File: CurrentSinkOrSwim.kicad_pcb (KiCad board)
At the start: 2 copper layers, 22 parts, among them P101 CONN_01X02, P102 CONN_01X03, P103 CONN_01X02, Q401 BUK9575, U201 LMV358, U301 LM2931D-R

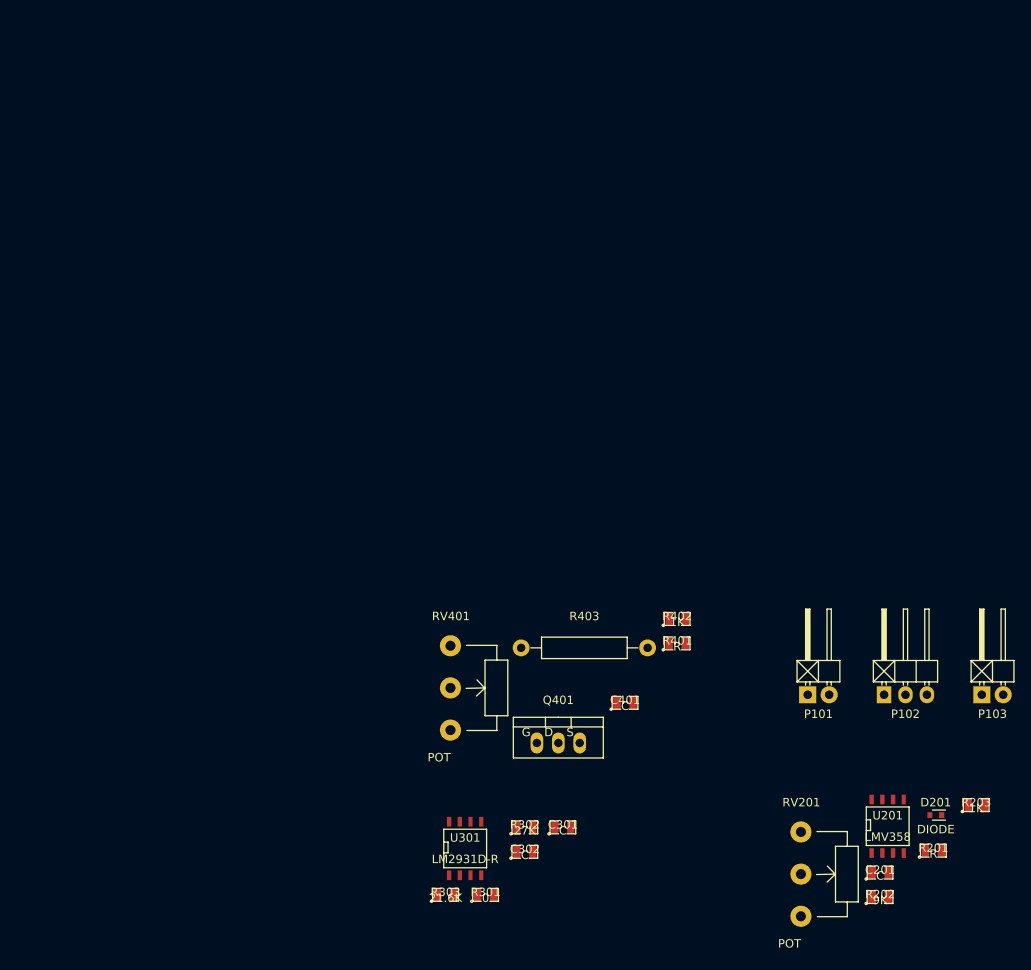
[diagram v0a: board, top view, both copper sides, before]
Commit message: Added board outline
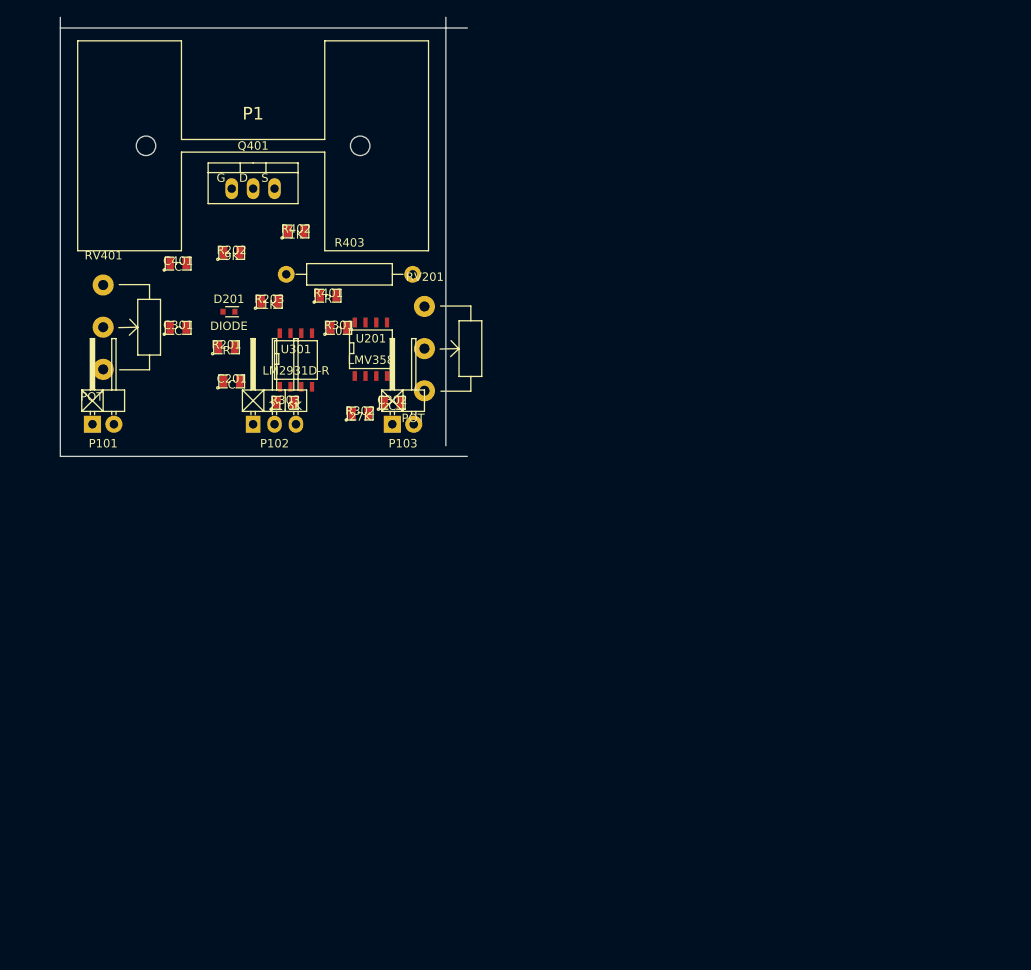
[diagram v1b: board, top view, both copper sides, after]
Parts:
- added P1: CONN_01X01, Current:FA-T220-38E, F.Cu at (127.0, 48.3)
- moved R202 108.4 mm to (124.5, 61.0)
- moved D201 102.9 mm to (124.1, 67.9)
- moved R201 102.9 mm to (123.8, 72.2)
- moved R203 102.9 mm to (128.9, 66.8)
- moved C201 96.5 mm to (124.5, 76.2)
- moved P101 90.7 mm to (109.2, 81.3)
- moved U201 83.4 mm to (141.0, 72.4)
- moved P102 81.4 mm to (129.5, 81.3)
- moved P103 76.9 mm to (144.8, 81.3)
- moved RV201 76.7 mm to (147.3, 67.3)
- moved Q401 75.0 mm to (127.0, 53.3)
- moved C301 74.8 mm to (118.1, 69.8)
- moved C401 74.3 mm to (118.1, 62.2)
- moved R301 69.5 mm to (137.2, 69.8)
- moved R402 64.5 mm to (132.1, 58.4)
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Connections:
- R302 pad 1: Net-(R302-Pad1) -> 2.7V
- U301 pad 5: Net-(U301-Pad5) -> Net-(R301-Pad1)
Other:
- board outline added: 48.3 x 52.1 mm

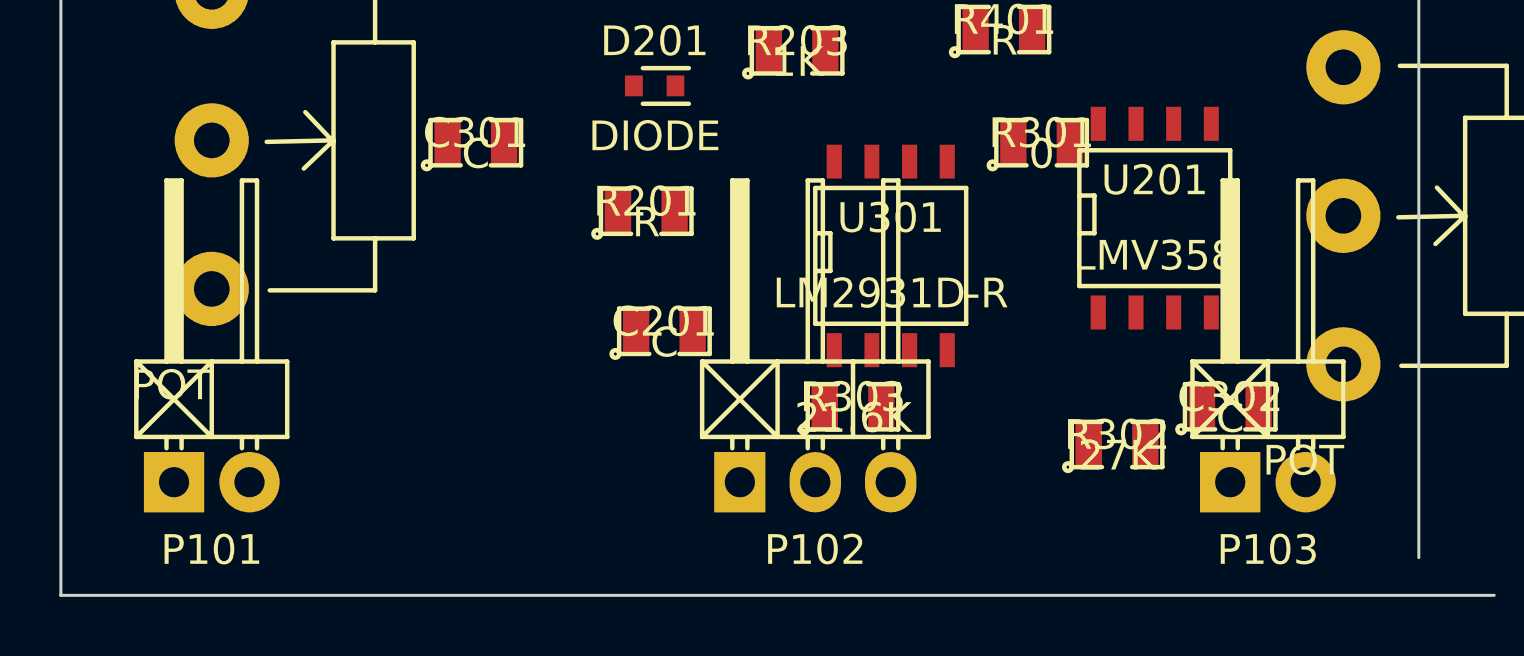
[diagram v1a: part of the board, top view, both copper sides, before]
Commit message: Replacing the terminal block footprints
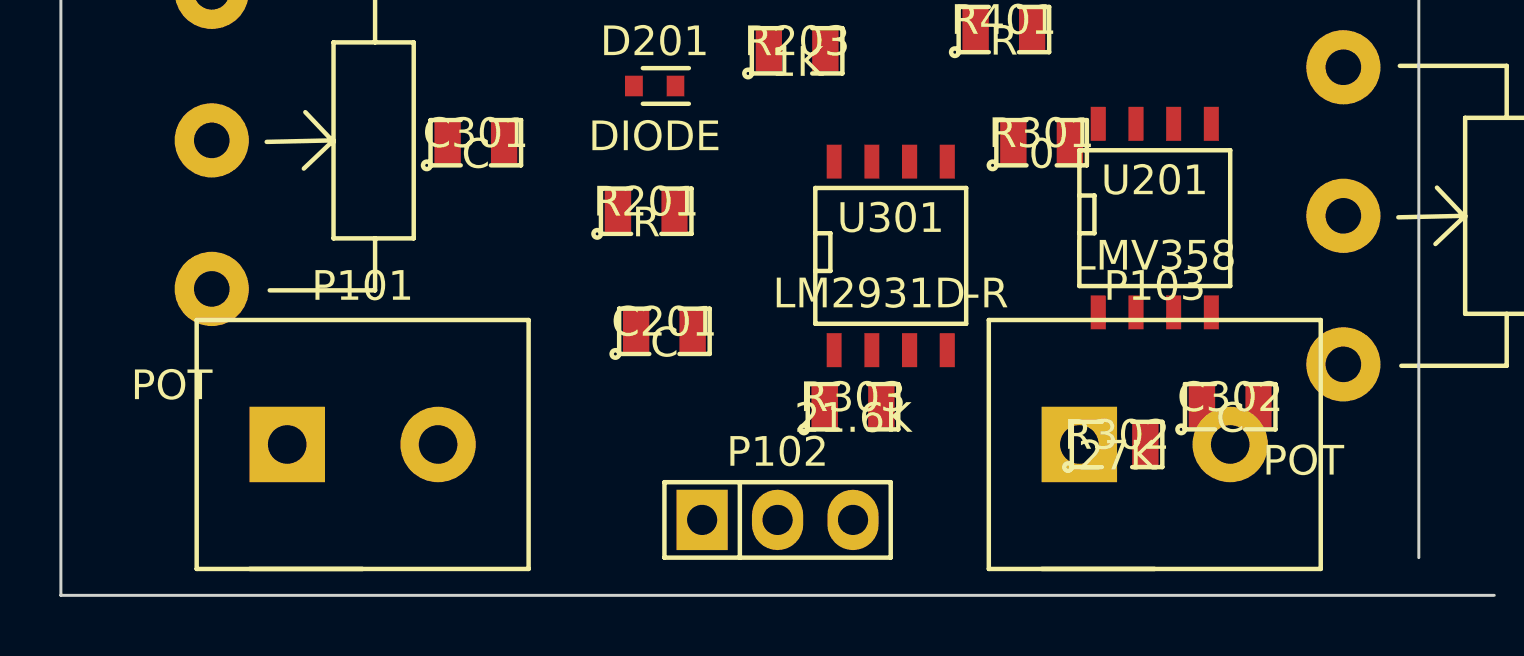
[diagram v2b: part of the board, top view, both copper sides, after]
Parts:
- P101, P103: footprint Pin_Headers:Pin_Header_Angled_1x02 -> Current:Terminal_Block_200_mil
- P102: footprint Pin_Headers:Pin_Header_Angled_1x03 -> Pin_Headers:Pin_Header_Straight_1x03
- moved P101 5.24 mm to (114.3, 80.0)
- moved P103 4.02 mm to (141.0, 80.0)
- moved P102 1.80 mm to (128.3, 82.5)
